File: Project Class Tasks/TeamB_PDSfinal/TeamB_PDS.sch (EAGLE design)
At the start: 23 parts, among them X1 remote_on_off

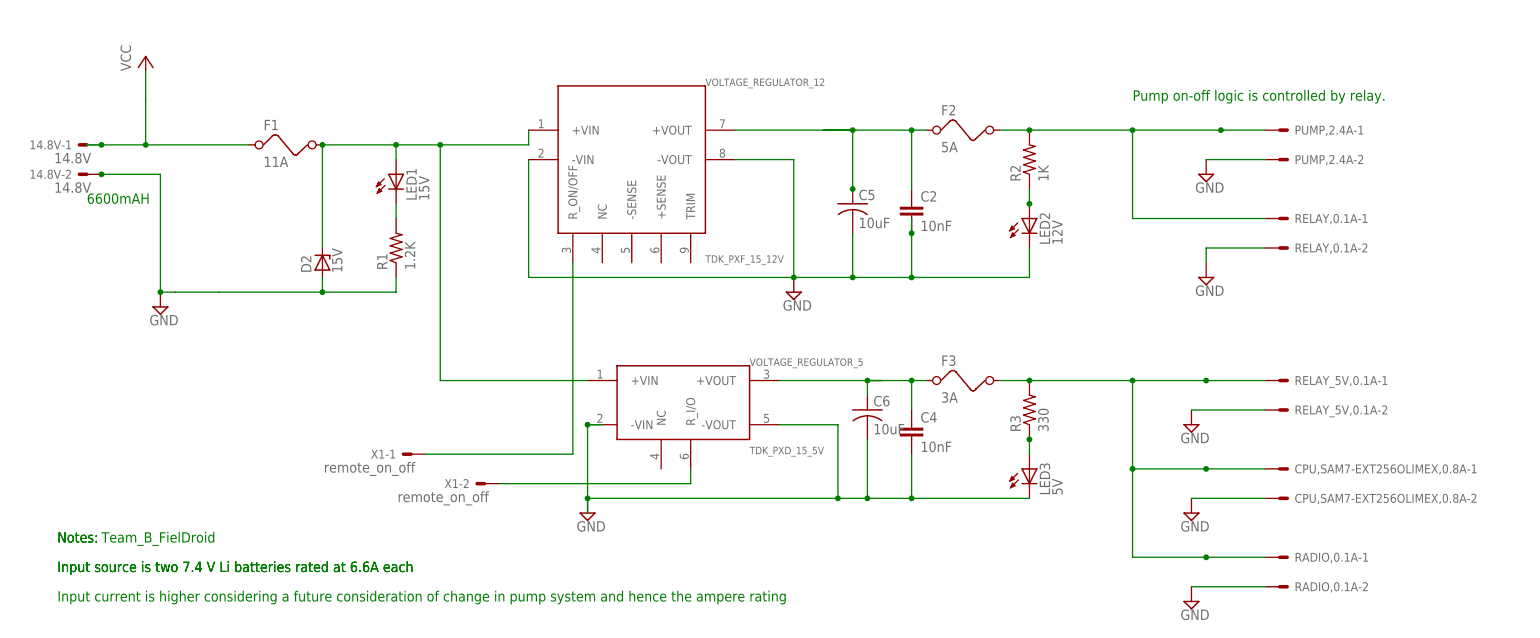
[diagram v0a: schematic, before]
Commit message: added Power distribution files submitted for TASK11
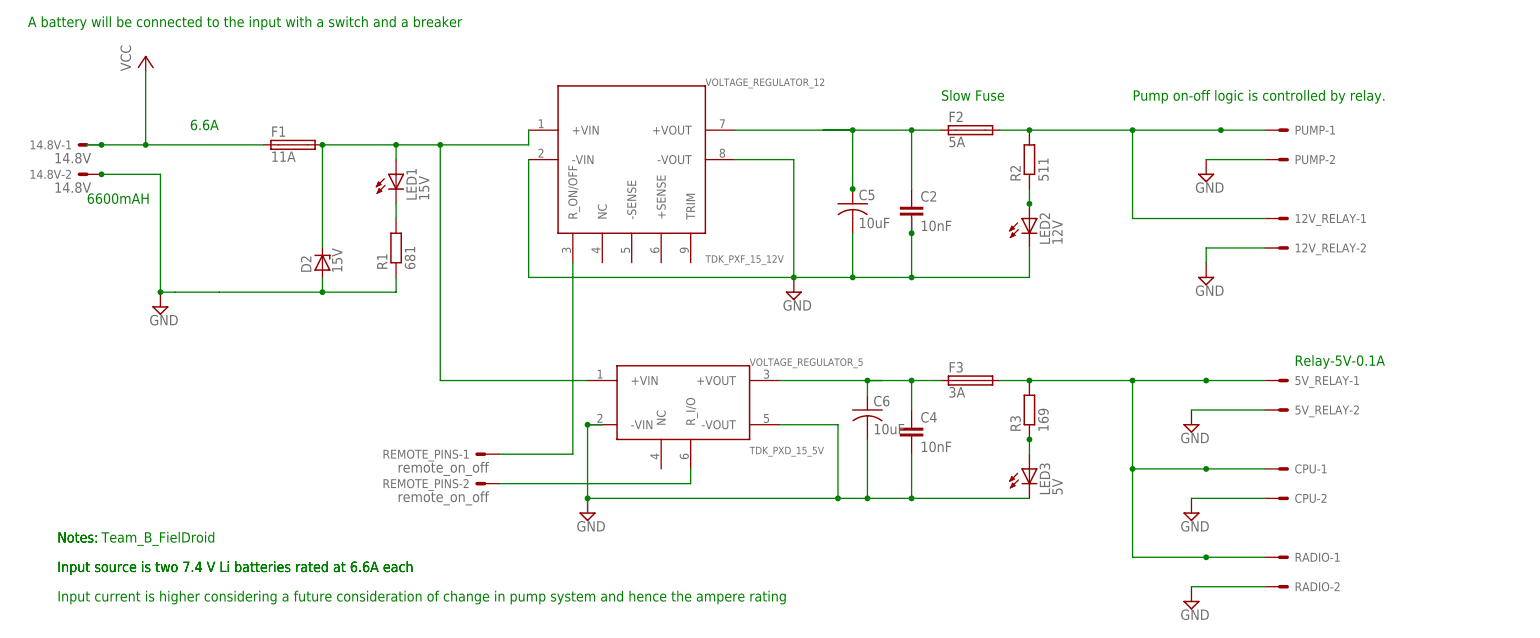
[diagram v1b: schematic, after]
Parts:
- removed X1: remote_on_off, con-molex:5566-2
- added REMOTE_PINS: remote_on_off, con-molex:5566-2
- C5, C6: device rcl:C-US050-045X075 -> rcl:C-US050-024X044
- D2: device diode:1N4728 -> diode:ZENER-DIODEZD-5
- F1, F2, F3: device special:FUSE -> fuse:FUSEBLANK_5X20MM
- R1: value 1.2K -> 681; device rcl:R-US_0309/12 -> rcl:R-EU_0204/7
- R2: value 1K -> 511; device rcl:R-US_0309/12 -> rcl:R-EU_0204/7
- R3: value 330 -> 169; device rcl:R-US_0309/12 -> rcl:R-EU_0204/7
- renumbered CPU,SAM7-EXT256OLIMEX,0.8A to CPU, PUMP,2.4A to PUMP, RADIO,0.1A to RADIO, RELAY,0.1A to 12V_RELAY, RELAY_5V,0.1A to 5V_RELAY
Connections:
- net N$6: now also REMOTE_PINS-1.S; no longer X1-1.S
- net N$7: now also REMOTE_PINS-2.S; no longer X1-2.S
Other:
- note added: "6.6A"
- note added: "A battery will be connected to the input with a switch and a breaker"
- note added: "Relay-5V-0.1A"
- note added: "Slow Fuse"
